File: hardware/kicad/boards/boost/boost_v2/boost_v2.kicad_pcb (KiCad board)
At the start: 2 copper layers, 104 x 104 mm, 17 parts, among them J1 lager ind (5V), J2 V2 ud (10V), J3 PWM (isoleret), J4 drive +15V, M1 IRF530, U1 CNY17, U2 IR2110

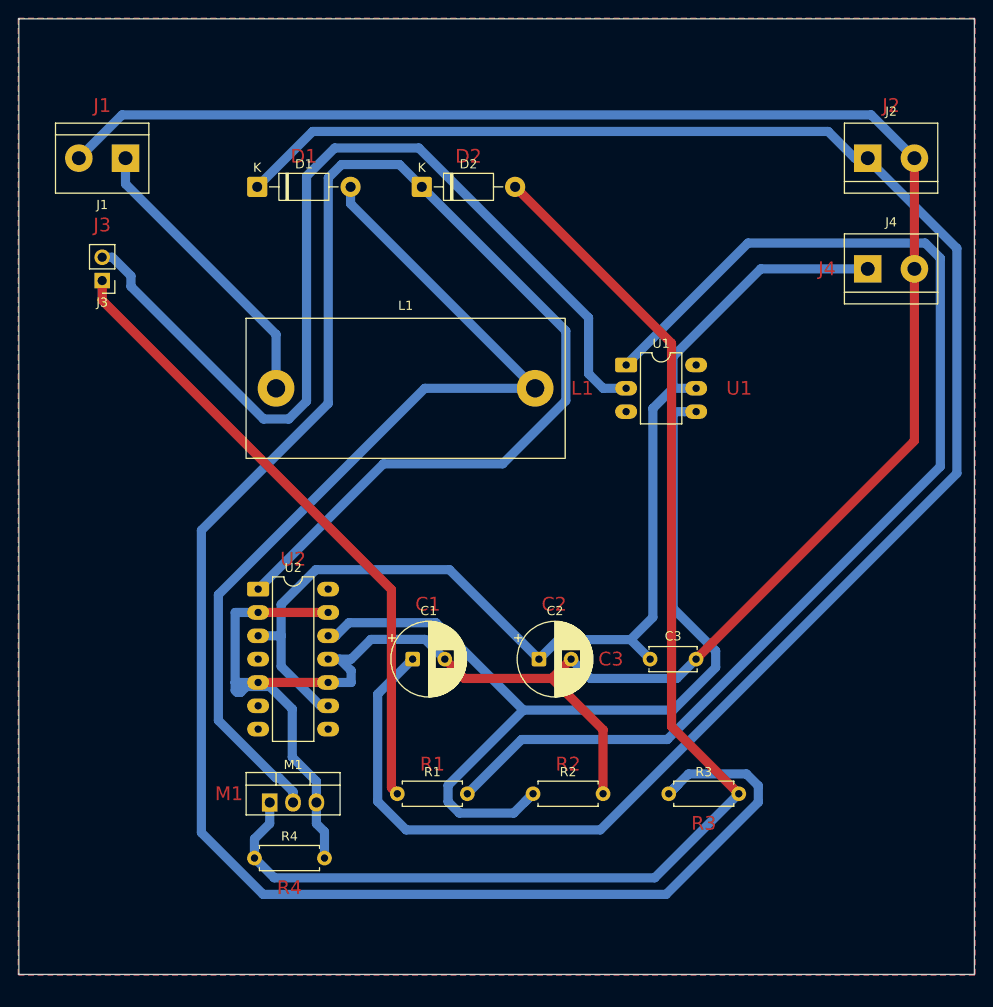
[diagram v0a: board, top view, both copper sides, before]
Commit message: Boost v2: faerdigt enkeltsidet layout + laser-DXF og maaleresultat
- boost_v2 board: enkeltsidet (kun B.Cu), ingen traadbroer eller vias
- produktion: DXF til laser (etch + huller), fjernet silk/top_cu
- rapport: boost maaleresultat 10 kHz 48%% -> 10.1 V, ~56 mV ripple + figur
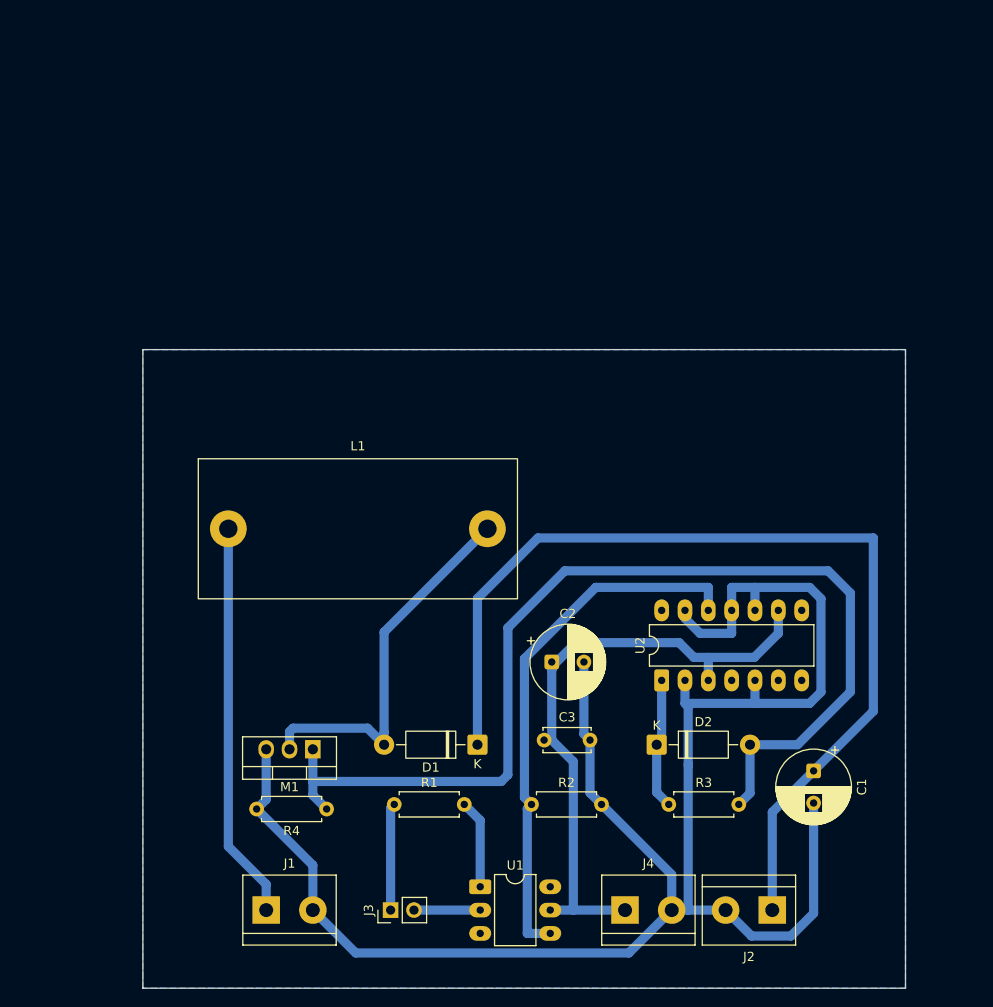
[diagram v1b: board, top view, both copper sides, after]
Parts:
- moved J1 83.3 mm to (46.9, 117.0), turned to 0 degrees
- moved J2 82.5 mm to (102.0, 117.0), turned to 180 degrees
- moved J3 75.4 mm to (60.5, 117.0), turned to 90 degrees
- moved J4 74.6 mm to (86.0, 117.0)
- moved D2 65.9 mm to (89.4, 99.0)
- moved D1 65.3 mm to (69.9, 99.0), turned to 180 degrees
- moved U1 59.0 mm to (70.2, 114.5)
- moved C1 45.3 mm to (106.5, 101.8), turned to -90 degrees
- moved U2 45.0 mm to (90.0, 92.0), turned to 90 degrees
- moved L1 16.1 mm to (42.8, 75.5)
- moved C3 14.5 mm to (77.2, 98.5)
- moved R4 9.50 mm to (53.5, 106.0), turned to 180 degrees
- moved M1 7.45 mm to (52.0, 99.5), turned to 180 degrees
- moved C2 1.43 mm to (78.0, 90.0)
- moved R1 1.21 mm to (60.9, 105.5)
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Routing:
- net /LO: track 242.6 -> 14.3 mm
- net /OPTO_A: track 129.3 -> 9.68 mm
- net VOUT_V2: track 206.0 -> 106.8 mm
- net GND_MCU: track 106.0 -> 7.21 mm
- net GND: track 278.9 -> 201.3 mm
- net /SW: track 100.2 -> 41.3 mm
- net PWM: track 69.2 -> 11.7 mm
- net +15V: track 124.0 -> 69.8 mm
- net /LIN: track 106.2 -> 58.6 mm
- net GATE: track 140.3 -> 116.6 mm
- net VIN_5V: track 31.8 -> 43.2 mm
- removed copper zone on F.Cu, net (none)
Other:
- board size 104 x 104 mm -> 83 x 69.5 mm
- board text removed: "C1"
- board text removed: "C2"
- board text removed: "C3"
- board text removed: "D1"
- board text removed: "D2"
- board text removed: "J1"
- board text removed: "J2"
- board text removed: "J3"
- board text removed: "J4"
- board text removed: "L1"
- board text removed: "M1"
- board text removed: "R1"
- board text removed: "R2"
- board text removed: "R3"
- board text removed: "R4"
- board text removed: "U1"
- board text removed: "U2"
